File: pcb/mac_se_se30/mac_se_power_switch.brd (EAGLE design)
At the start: 27.1 x 59 mm, 5 parts

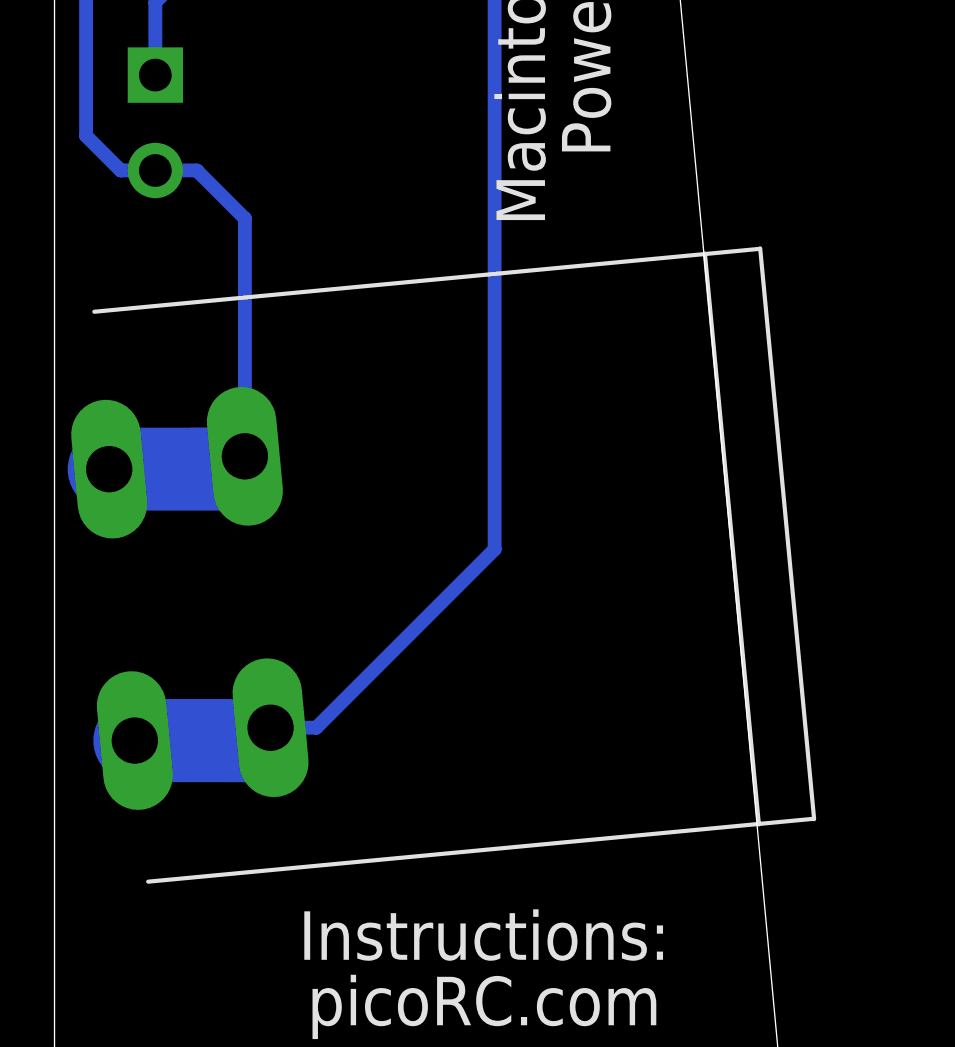
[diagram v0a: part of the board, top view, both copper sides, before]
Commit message: updated switch location
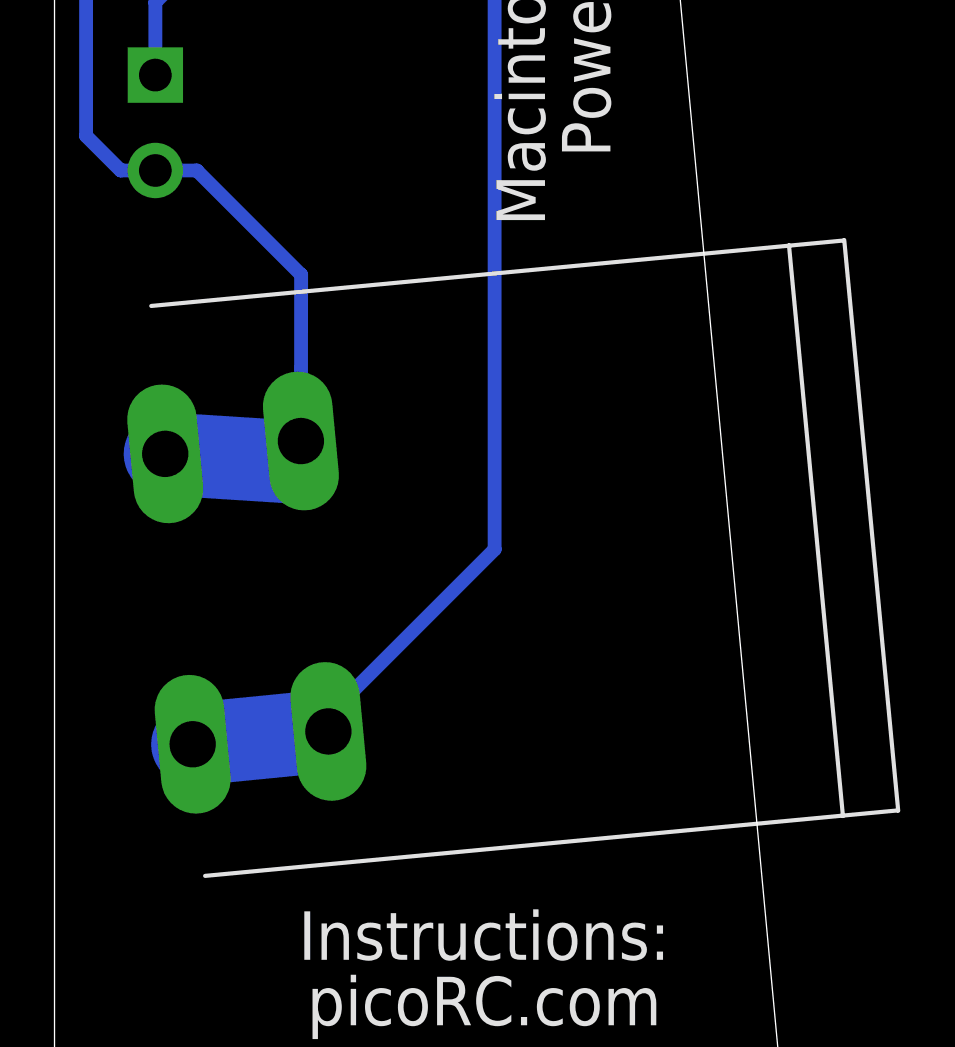
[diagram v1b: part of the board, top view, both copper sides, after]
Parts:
- moved U$1 2.10 mm to (-2.46, 21.3)
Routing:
- net N$3: track 52.9 -> 51.1 mm
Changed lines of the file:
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@@
 <setting verticaltext="up"/>
 </settings>
-<grid distance="10" unitdist="mil" unit="mil" style="lines" multiple="1" display="no" altdistance="1" altunitdist="mil" altunit="mil"/>
+<grid distance="0.000123031496" unitdist="mil" unit="mil" style="lines" multiple="1" display="no" altdistance="1" altunitdist="mil" altunit="mil"/>
 <layers>
 <layer number="1" name="Top" color="4" fill="1" visible="yes" active="yes"/>
@@
 <element name="U$2" library="a" package="M3_MOUNTING_HOLE_PACK" value="M3_MOUNTING_HOLE" x="0" y="0" smashed="yes"/>
 <element name="U$3" library="a" package="M3_MOUNTING_HOLE_PACK" value="M3_MOUNTING_HOLE" x="0" y="53" smashed="yes"/>
-<element name="U$1" library="atx4vc" package="ROCK_SWITCH" value="ROCK_SW" x="-4.5522" y="21.1234" smashed="yes" rot="R275.4"/>
+<element name="U$1" library="atx4vc" package="ROCK_SWITCH" value="ROCK_SW" x="-2.4638" y="21.336" smashed="yes" rot="R275.4"/>
 </elements>
 <signals>
@@
 <contactref element="J7" pad="2"/>
 <contactref element="JP2" pad="2"/>
-<wire x1="-4.99450625" y1="25.802540625" x2="-0.68935" y2="25.8055125" width="3.048" layer="16"/>
+<wire x1="-2.939046875" y1="26.3635875" x2="1.3832375" y2="26.08751875" width="3.048" layer="16"/>
 <wire x1="-3.302" y1="36.759" x2="-1.778" y2="36.759" width="0.508" layer="16"/>
 <wire x1="-3.302" y1="36.759" x2="-4.572" y2="36.759" width="0.508" layer="16"/>
@@
 <wire x1="-5.842" y1="43.688" x2="-1.397" y2="48.133" width="0.508" layer="16"/>
 <wire x1="-1.397" y1="48.133" x2="4.572" y2="48.133" width="0.508" layer="16"/>
-<wire x1="-0.016696875" y1="34.997696875" x2="-0.016696875" y2="26.27308125" width="0.508" layer="16"/>
-<wire x1="-1.778" y1="36.759" x2="-0.016696875" y2="34.997696875" width="0.508" layer="16"/>
-<wire x1="-0.68935" y1="25.8055125" x2="-0.016696875" y2="26.27308125" width="0" layer="19" extent="16-16"/>
+<wire x1="2.04666875" y1="32.93433125" x2="2.038765625" y2="26.834128125" width="0.508" layer="16"/>
+<wire x1="-1.778" y1="36.759" x2="2.04666875" y2="32.93433125" width="0.508" layer="16"/>
+<wire x1="1.3832375" y1="26.08751875" x2="2.038765625" y2="26.834128125" width="0" layer="19" extent="16-16"/>
 </signal>
 <signal name="N$3">
@@
 <contactref element="J7" pad="1"/>
 <contactref element="JP2" pad="1"/>
-<wire x1="-4.053425" y1="15.84691875" x2="0.182203125" y2="15.843565625" width="3.048" layer="16"/>
+<wire x1="-1.9320875" y1="15.711071875" x2="2.254790625" y2="16.125571875" width="3.048" layer="16"/>
 <wire x1="-3.302" y1="40.259" x2="-3.302" y2="42.926" width="0.508" layer="16"/>
 <wire x1="-0.635" y1="45.593" x2="4.572" y2="45.593" width="0.508" layer="16"/>
@@
 <wire x1="6.985" y1="45.593" x2="9.144" y2="43.434" width="0.508" layer="16"/>
 <wire x1="9.144" y1="22.86" x2="9.144" y2="43.434" width="0.508" layer="16"/>
-<wire x1="0.92438125" y1="16.3174625" x2="2.6014625" y2="16.3174625" width="0.508" layer="16"/>
-<wire x1="2.6014625" y1="16.3174625" x2="9.144" y2="22.86" width="0.508" layer="16"/>
-<wire x1="0.182203125" y1="15.843565625" x2="0.92438125" y2="16.3174625" width="0" layer="19" extent="16-16"/>
+<wire x1="3.04571875" y1="16.181615625" x2="3.16299375" y2="16.87899375" width="0.508" layer="16"/>
+<wire x1="3.16299375" y1="16.87899375" x2="9.144" y2="22.86" width="0.508" layer="16"/>
+<wire x1="2.254790625" y1="16.125571875" x2="3.04571875" y2="16.181615625" width="0" layer="19" extent="16-16"/>
 </signal>
 </signals>

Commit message: updated pcb
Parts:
- moved U$1 4.78 mm to (2.31, 21.3)
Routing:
- net N$3: track 51.1 -> 57.4 mm
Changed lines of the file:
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@@
 <setting verticaltext="up"/>
 </settings>
-<grid distance="0.000123031496" unitdist="mil" unit="mil" style="lines" multiple="1" display="no" altdistance="1" altunitdist="mil" altunit="mil"/>
+<grid distance="0.25" unitdist="mm" unit="mm" style="lines" multiple="1" display="no" altdistance="1" altunitdist="mil" altunit="mil"/>
 <layers>
 <layer number="1" name="Top" color="4" fill="1" visible="yes" active="yes"/>
@@
 Dec 2022</text>
 <wire x1="14.7334" y1="56.8706" x2="20.3722" y2="-3.8862" width="0.1524" layer="51"/>
+<wire x1="9.44913125" y1="32.508409375" x2="44.948671875" y2="35.83150625" width="0.1524" layer="25"/>
 </plain>
 <attributes>
@@
 <element name="U$2" library="a" package="M3_MOUNTING_HOLE_PACK" value="M3_MOUNTING_HOLE" x="0" y="0" smashed="yes"/>
 <element name="U$3" library="a" package="M3_MOUNTING_HOLE_PACK" value="M3_MOUNTING_HOLE" x="0" y="53" smashed="yes"/>
-<element name="U$1" library="atx4vc" package="ROCK_SWITCH" value="ROCK_SW" x="-2.4638" y="21.336" smashed="yes" rot="R275.4"/>
+<element name="U$1" library="atx4vc" package="ROCK_SWITCH" value="ROCK_SW" x="2.31186875" y="21.302290625" smashed="yes" rot="R275.4"/>
 </elements>
 <signals>
@@
 <contactref element="J7" pad="2"/>
 <contactref element="JP2" pad="2"/>
-<wire x1="-2.939046875" y1="26.3635875" x2="1.3832375" y2="26.08751875" width="3.048" layer="16"/>
+<wire x1="1.836621875" y1="26.329878125" x2="6.15890625" y2="26.053809375" width="3.048" layer="16"/>
 <wire x1="-3.302" y1="36.759" x2="-1.778" y2="36.759" width="0.508" layer="16"/>
 <wire x1="-3.302" y1="36.759" x2="-4.572" y2="36.759" width="0.508" layer="16"/>
@@
 <wire x1="2.04666875" y1="32.93433125" x2="2.038765625" y2="26.834128125" width="0.508" layer="16"/>
 <wire x1="-1.778" y1="36.759" x2="2.04666875" y2="32.93433125" width="0.508" layer="16"/>
-<wire x1="1.3832375" y1="26.08751875" x2="2.038765625" y2="26.834128125" width="0" layer="19" extent="16-16"/>
+<wire x1="6.15890625" y1="26.053809375" x2="6.81443125" y2="26.80041875" width="0" layer="19" extent="16-16"/>
+<wire x1="2.038765625" y1="26.834128125" x2="1.836621875" y2="26.329878125" width="0" layer="19" extent="16-16"/>
 </signal>
 <signal name="N$3">
@@
 <contactref element="J7" pad="1"/>
 <contactref element="JP2" pad="1"/>
-<wire x1="-1.9320875" y1="15.711071875" x2="2.254790625" y2="16.125571875" width="3.048" layer="16"/>
+<wire x1="2.84358125" y1="15.6773625" x2="7.030459375" y2="16.0918625" width="3.048" layer="16"/>
 <wire x1="-3.302" y1="40.259" x2="-3.302" y2="42.926" width="0.508" layer="16"/>
 <wire x1="-0.635" y1="45.593" x2="4.572" y2="45.593" width="0.508" layer="16"/>
@@
 <wire x1="4.572" y1="45.593" x2="6.985" y2="45.593" width="0.508" layer="16"/>
 <wire x1="6.985" y1="45.593" x2="9.144" y2="43.434" width="0.508" layer="16"/>
-<wire x1="9.144" y1="22.86" x2="9.144" y2="43.434" width="0.508" layer="16"/>
-<wire x1="3.04571875" y1="16.181615625" x2="3.16299375" y2="16.87899375" width="0.508" layer="16"/>
-<wire x1="3.16299375" y1="16.87899375" x2="9.144" y2="22.86" width="0.508" layer="16"/>
-<wire x1="2.254790625" y1="16.125571875" x2="3.04571875" y2="16.181615625" width="0" layer="19" extent="16-16"/>
+<wire x1="-3.302" y1="40.259" x2="4.318" y2="40.259" width="0.508" layer="16"/>
+<wire x1="4.318" y1="40.259" x2="11.303" y2="33.274" width="0.508" layer="16"/>
+<wire x1="11.303" y1="33.274" x2="11.303" y2="19.62951875" width="0.508" layer="16"/>
+<wire x1="11.303" y1="19.62951875" x2="7.8213875" y2="16.14790625" width="0.508" layer="16"/>
+<wire x1="7.030459375" y1="16.0918625" x2="7.8213875" y2="16.14790625" width="0" layer="19" extent="16-16"/>
 </signal>
 </signals>

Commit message: updated pcb
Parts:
- removed J7: (no value), atx_power_control:SCREWTERMINAL-3.5MM-2-NS
- moved JP2 5.27 mm to (0.26, 41.6)
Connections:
- net N$2: no longer J7.2
- net N$3: no longer J7.1
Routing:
- net N$3: track 57.4 -> 34.5 mm
- net N$2: track 38.3 -> 24.9 mm
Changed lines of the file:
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@@
 <setting verticaltext="up"/>
 </settings>
-<grid distance="0.25" unitdist="mm" unit="mm" style="lines" multiple="1" display="no" altdistance="1" altunitdist="mil" altunit="mil"/>
+<grid distance="10" unitdist="mil" unit="mil" style="lines" multiple="1" display="no" altdistance="1" altunitdist="mil" altunit="mil"/>
 <layers>
 <layer number="1" name="Top" color="4" fill="1" visible="yes" active="yes"/>
@@
 <text x="8.763" y="7.493" size="1.778" layer="25" distance="35" rot="R180" align="center">Instructions:
 picoRC.com</text>
-<text x="11.303" y="44.577" size="1.778" layer="25" distance="35" rot="R270" align="center">Macintosh SE ATX
+<text x="10.541" y="43.815" size="1.778" layer="25" distance="35" rot="R270" align="center">Macintosh SE ATX
 Power Switch</text>
 <text x="10.541" y="1.27" size="1.4224" layer="25" distance="30" align="center">PT2 dekuNukem
@@
 </autorouter>
 <elements>
-<element name="J7" library="atx_power_control" package="SCREWTERMINAL-3.5MM-2-NS" value="" x="-3.302" y="40.259" smashed="yes" rot="R270">
-<attribute name="PROD_ID" value="CONN-13512" x="-3.302" y="40.259" size="1.778" layer="27" rot="R270" display="off"/>
-<attribute name="SF_ID" value="PRT-09918" x="-3.302" y="40.259" size="1.778" layer="27" rot="R270" display="off"/>
-<attribute name="SF_SKU" value="PRT-08432" x="-3.302" y="40.259" size="1.778" layer="27" rot="R270" display="off"/>
-<attribute name="SKU" value="PRT-09914" x="-3.302" y="40.259" size="1.778" layer="27" rot="R270" display="off"/>
-<attribute name="VALUE" x="-2.032" y="41.529" size="0.6096" layer="27" font="vector" ratio="20" rot="R270"/>
-</element>
-<element name="JP2" library="pinhead" library_urn="urn:adsk.eagle:library:325" package="1X02/90" package3d_urn="urn:adsk.eagle:package:22437/2" value="" x="0.762" y="46.863" smashed="yes" rot="R90">
-<attribute name="POPULARITY" value="24" x="0.762" y="46.863" size="1.778" layer="27" rot="R90" display="off"/>
-<attribute name="VALUE" x="3.937" y="44.323" size="1.27" layer="27" rot="R90"/>
+<element name="JP2" library="pinhead" library_urn="urn:adsk.eagle:library:325" package="1X02/90" package3d_urn="urn:adsk.eagle:package:22437/2" value="" x="0.262" y="41.613" smashed="yes" rot="R90">
+<attribute name="POPULARITY" value="24" x="0.262" y="41.613" size="1.778" layer="27" rot="R90" display="off"/>
+<attribute name="VALUE" x="3.437" y="39.073" size="1.27" layer="27" rot="R90"/>
 </element>
 <element name="U$2" library="a" package="M3_MOUNTING_HOLE_PACK" value="M3_MOUNTING_HOLE" x="0" y="0" smashed="yes"/>
@@
 <contactref element="U$1" pad="P$3"/>
 <contactref element="U$1" pad="P$1"/>
-<contactref element="J7" pad="2"/>
 <contactref element="JP2" pad="2"/>
 <wire x1="1.836621875" y1="26.329878125" x2="6.15890625" y2="26.053809375" width="3.048" layer="16"/>
-<wire x1="-3.302" y1="36.759" x2="-1.778" y2="36.759" width="0.508" layer="16"/>
-<wire x1="-3.302" y1="36.759" x2="-4.572" y2="36.759" width="0.508" layer="16"/>
-<wire x1="-4.572" y1="36.759" x2="-5.842" y2="38.029" width="0.508" layer="16"/>
-<wire x1="-5.842" y1="38.029" x2="-5.842" y2="43.688" width="0.508" layer="16"/>
-<wire x1="-5.842" y1="43.688" x2="-1.397" y2="48.133" width="0.508" layer="16"/>
-<wire x1="-1.397" y1="48.133" x2="4.572" y2="48.133" width="0.508" layer="16"/>
-<wire x1="2.04666875" y1="32.93433125" x2="2.038765625" y2="26.834128125" width="0.508" layer="16"/>
-<wire x1="-1.778" y1="36.759" x2="2.04666875" y2="32.93433125" width="0.508" layer="16"/>
+<wire x1="4.072" y1="42.883" x2="1.735" y2="42.883" width="0.508" layer="16"/>
+<wire x1="1.735" y1="42.883" x2="-0.254" y2="40.894" width="0.508" layer="16"/>
+<wire x1="-0.254" y1="40.894" x2="-0.254" y2="28.4205" width="0.508" layer="16"/>
+<wire x1="-0.254" y1="28.4205" x2="1.836621875" y2="26.329878125" width="0.508" layer="16"/>
 <wire x1="6.15890625" y1="26.053809375" x2="6.81443125" y2="26.80041875" width="0" layer="19" extent="16-16"/>
-<wire x1="2.038765625" y1="26.834128125" x2="1.836621875" y2="26.329878125" width="0" layer="19" extent="16-16"/>
+<wire x1="1.83661875" y1="26.329878125" x2="6.15890625" y2="26.053809375" width="0" layer="19" extent="16-16"/>
 </signal>
 <signal name="N$3">
 <contactref element="U$1" pad="P$4"/>
 <contactref element="U$1" pad="P$2"/>
-<contactref element="J7" pad="1"/>
 <contactref element="JP2" pad="1"/>
 <wire x1="2.84358125" y1="15.6773625" x2="7.030459375" y2="16.0918625" width="3.048" layer="16"/>
-<wire x1="-3.302" y1="40.259" x2="-3.302" y2="42.926" width="0.508" layer="16"/>
-<wire x1="-0.635" y1="45.593" x2="4.572" y2="45.593" width="0.508" layer="16"/>
-<wire x1="-3.302" y1="42.926" x2="-0.635" y2="45.593" width="0.508" layer="16"/>
-<wire x1="4.572" y1="45.593" x2="6.985" y2="45.593" width="0.508" layer="16"/>
-<wire x1="6.985" y1="45.593" x2="9.144" y2="43.434" width="0.508" layer="16"/>
-<wire x1="-3.302" y1="40.259" x2="4.318" y2="40.259" width="0.508" layer="16"/>
-<wire x1="4.318" y1="40.259" x2="11.303" y2="33.274" width="0.508" layer="16"/>
-<wire x1="11.303" y1="33.274" x2="11.303" y2="19.62951875" width="0.508" layer="16"/>
-<wire x1="11.303" y1="19.62951875" x2="7.8213875" y2="16.14790625" width="0.508" layer="16"/>
+<wire x1="7.8213875" y1="16.14790625" x2="11.303" y2="19.62951875" width="0.508" layer="16"/>
+<wire x1="6.901" y1="40.343" x2="4.072" y2="40.343" width="0.508" layer="16"/>
+<wire x1="11.303" y1="19.62951875" x2="11.303" y2="35.941" width="0.508" layer="16"/>
+<wire x1="11.303" y1="35.941" x2="6.901" y2="40.343" width="0.508" layer="16"/>
 <wire x1="7.030459375" y1="16.0918625" x2="7.8213875" y2="16.14790625" width="0" layer="19" extent="16-16"/>
+<wire x1="2.843578125" y1="15.6773625" x2="2.84358125" y2="15.6773625" width="0" layer="19" extent="16-16"/>
 </signal>
 </signals>
